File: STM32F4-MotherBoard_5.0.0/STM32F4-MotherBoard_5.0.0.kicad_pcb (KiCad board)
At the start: 2 copper layers, 95 parts, among them J1 RJ45, J2 RJ45, J3 RJ12, J4 RJ12, P1 VCC, P2 GND, P3 DIO0, P4 ADC, P5 DIO1, P6 SWD, P7 ENC0, P8 ENC2, P9 ENC1, SW1 ON/OFF, SW2 Reset, SW3 SW_PUSH, SW4 SW_ROTARY, SW5 WRITE/RUN, U1 STM32F407VG, U2 OKL-T6-W12, U3 PQ033EZ1H, U4 MCP2551-I/SN, U5 ADM3202, U6 AS021350D, Y1 8MHz

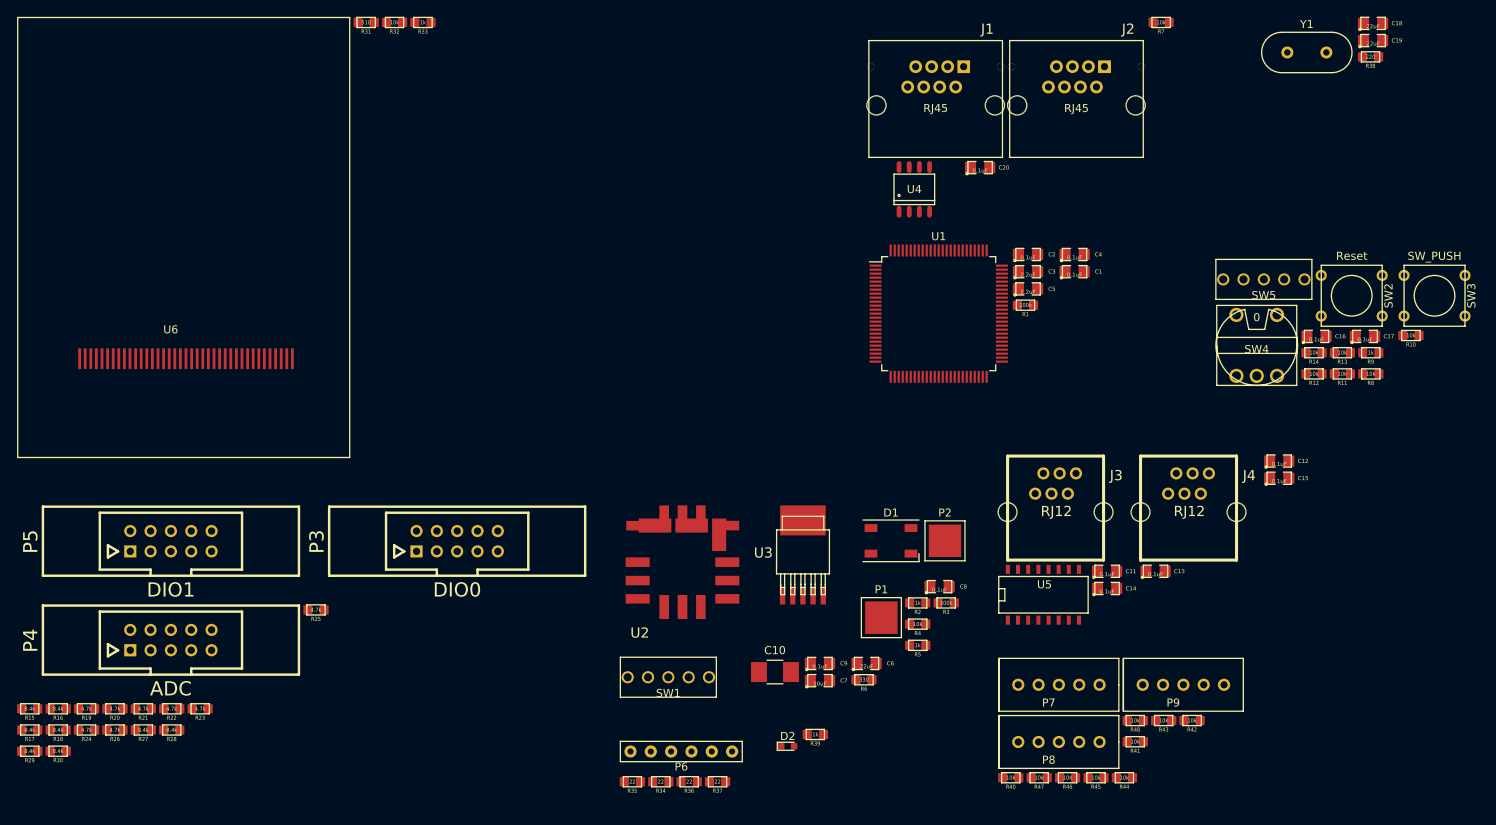
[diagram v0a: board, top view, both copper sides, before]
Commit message: 部品配置終わり
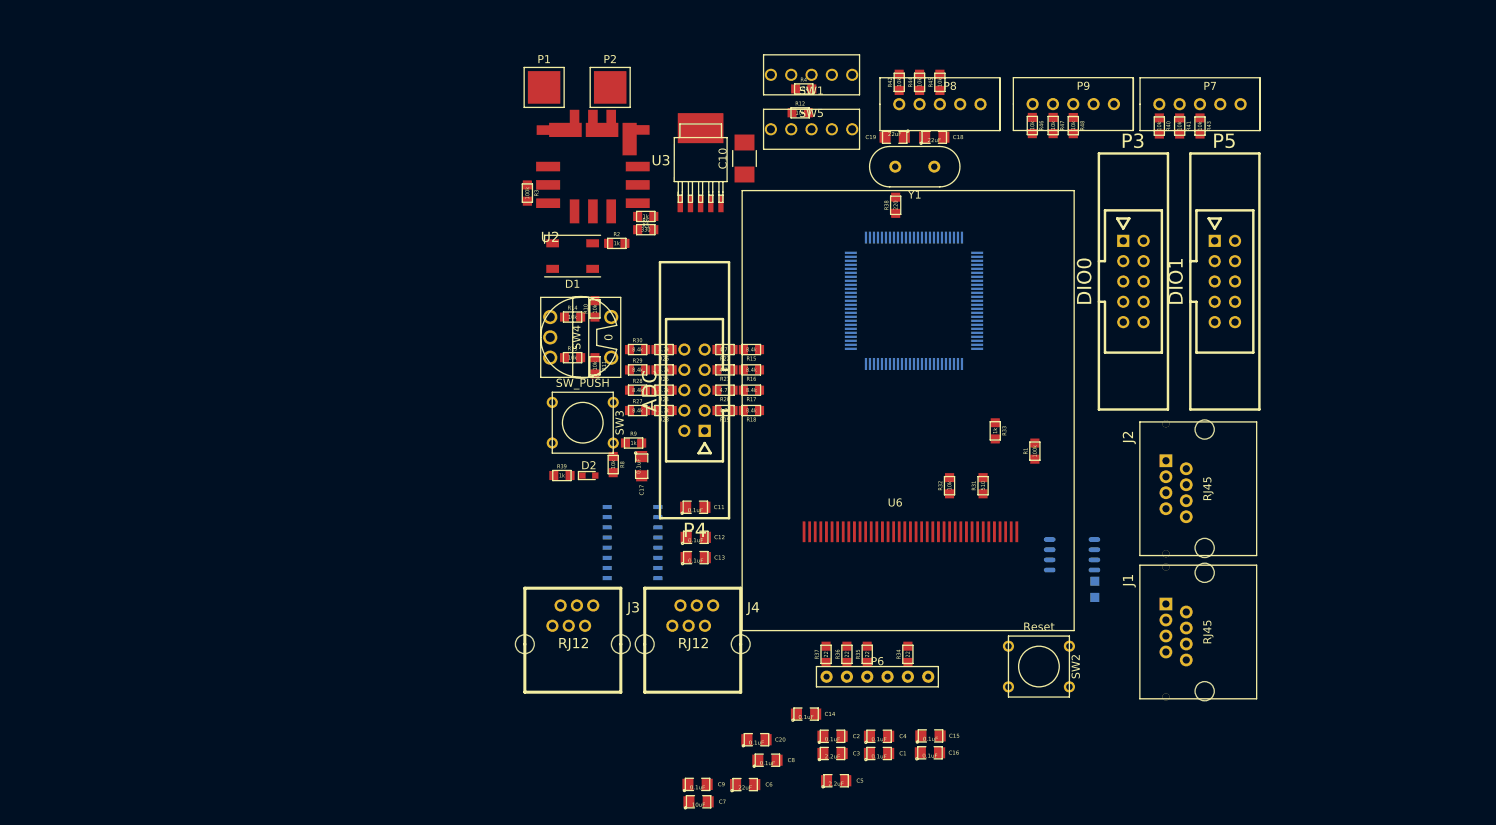
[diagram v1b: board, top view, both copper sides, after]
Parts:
- R7, U1, U4, U5: moved to B.Cu
- moved P5 135.7 mm to (204.5, 66.7), turned to 270 degrees
- moved SW3 107.6 mm to (124.2, 84.3)
- moved R10 102.1 mm to (125.7, 70.1), turned to 270 degrees
- moved R15 100.8 mm to (145.3, 75.2)
- moved R17 99.7 mm to (145.3, 80.3)
- moved R16 96.5 mm to (145.3, 77.7)
- moved R31 96.4 mm to (174.2, 92.2), turned to 270 degrees
- moved R13 96.2 mm to (122.9, 76.2), turned to 180 degrees
- moved R18 95.4 mm to (145.3, 82.8)
- moved R8 95.4 mm to (128.0, 89.6), turned to 90 degrees
- moved R11 93.4 mm to (125.7, 77.2), turned to 90 degrees
- moved U6 93.1 mm to (151.1, 99.3)
- moved R9 92.8 mm to (130.6, 86.9), turned to 180 degrees
- moved R14 92.8 mm to (122.9, 71.1), turned to 180 degrees
- moved C17 91.9 mm to (131.6, 89.8), turned to 270 degrees
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
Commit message: 部品配置再考終わり
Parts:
- added REF**: 1pin, Connect:1pin, F.Cu at (163.8, 50.8)
- added REF**: 1pin, Connect:1pin, F.Cu at (163.8, 127.0)
- added REF**: 1pin, Connect:1pin, F.Cu at (75.6, 50.8)
- added REF**: 1pin, Connect:1pin, F.Cu at (75.6, 127.0)
- C11, C12, C13, C14, C3, R1, R12, R15, R16, R17, R18, R19, R20, R21, R22, R23, R24, R25, R26, R27, R28, R29, R30, R38, R4, R40, R41, R42, R43, R44, R45: moved to B.Cu
- R7, U4: moved to F.Cu
- moved P5 123.7 mm to (83.2, 90.6), turned to 90 degrees
- moved P3 101.3 mm to (94.5, 90.4), turned to 90 degrees
- moved C6 98.9 mm to (75.6, 58.6), turned to 180 degrees
- moved C15 85.9 mm to (98.7, 72.2), turned to 180 degrees
- moved C1 85.2 mm to (101.5, 64.9), turned to 270 degrees
- moved C20 82.4 mm to (91.9, 61.8), turned to 270 degrees
- moved C8 81.9 mm to (91.6, 66.4), turned to 270 degrees
- moved P7 81.1 mm to (120.7, 52.7), turned to 0 degrees
- moved R43 81.1 mm to (120.7, 55.3)
- moved C2 76.9 mm to (105.6, 64.9), turned to 270 degrees
- moved R41 76.1 mm to (123.2, 55.3)
- moved C7 74.6 mm to (93.8, 72.2), turned to 180 degrees
- moved C9 73.5 mm to (103.5, 64.9), turned to 270 degrees
- moved R40 71.0 mm to (125.7, 55.4)
- moved R14 66.0 mm to (78.6, 120.0), turned to 0 degrees
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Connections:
- C20 pad 1: +5VP -> +5V
- U4 pad 3: +5VP -> +5V
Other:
- board outline added: 95.9 x 83.8 mm
- net class Default: clearance 0.2 -> 0.15; trace_width 0.25 -> 0.203
- rule trace_clearance: 0.2 -> 0.15

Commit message: ミス
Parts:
- ? (x4): renamed from REF**; value 1pin -> (none)
- C4: moved to B.Cu
- moved C4 16.5 mm to (137.3, 116.2)
- moved C5 13.7 mm to (105.6, 102.2), turned to 225 degrees
- moved R33 10.8 mm to (133.9, 109.7), turned to 270 degrees
- moved C3 6.41 mm to (132.3, 94.1), turned to 225 degrees
- moved R8 5.02 mm to (80.4, 112.2)
- moved R10 2.05 mm to (92.2, 121.0), turned to 90 degrees
- moved R31 1.76 mm to (133.9, 106.2)
- moved C17 1.14 mm to (78.4, 111.9)
- moved R1 0.97 mm to (138.0, 85.7)
- moved R9 0.82 mm to (79.4, 115.1), turned to 0 degrees
- moved + 0.57 mm to (79.4, 55.1)
- moved R4 0.30 mm to (105.7, 53.4)
- turned P5 to 270 degrees
- turned P3 to 270 degrees
- renumbered P1 to +, P2 to -, J1 to CAN, J2 to CAN, J4 to Communication, J3 to Controller, P7 to ENC0, P9 to ENC1, P8 to ENC2, D2 to LED, SW1 to ON/OFF, D1 to Pow, P6 to ST-Link, SW5 to WRITE/RUN
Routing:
- net +3V3: track 0.00 -> 503.4 mm, vias 0 -> 12
- net GND: track 0.00 -> 211.4 mm, vias 0 -> 12
- net +5V: track 0.00 -> 208.9 mm, vias 0 -> 3
- net +12V: track 0.00 -> 136.4 mm
- net RotarySW2: track 0.00 -> 90.6 mm, vias 0 -> 2
- net RotarySW3: track 0.00 -> 84.8 mm, vias 0 -> 2
- net ADC4: track 0.00 -> 83.0 mm, vias 0 -> 2
- net ADC5: track 0.00 -> 77.8 mm, vias 0 -> 2
- net SWO: track 0.00 -> 71.3 mm, vias 0 -> 3
- net PushSW: track 0.00 -> 71.2 mm, vias 0 -> 3
- net ADC2: track 0.00 -> 70.8 mm, vias 0 -> 2
- net ENC2_Z: track 0.00 -> 69.2 mm, vias 0 -> 2
- net ADC6: track 0.00 -> 66.3 mm, vias 0 -> 2
- net ADC0: track 0.00 -> 66.2 mm, vias 0 -> 2
- net ADC1: track 0.00 -> 66.1 mm, vias 0 -> 2
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- added copper zone on B.Cu, net GND
- added copper zone on F.Cu, net GND
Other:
- board text added: "Designed with KiCAD by mugi"

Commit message: replace project
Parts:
- added J5: DM3AT-SF-PEJM5, HRS_DM3AT-SF-PEJM5, B.Cu at (125.0, 114.4)
- LED: value LED -> (none)
- moved R27 2.94 mm to (106.6, 113.0)
- moved R20 2.94 mm to (109.1, 124.5)
- moved R19 2.94 mm to (106.6, 124.5)
- moved R21 2.94 mm to (111.6, 124.5)
- moved R23 2.94 mm to (106.6, 116.6)
- moved R22 2.94 mm to (114.2, 124.5)
- moved R17 2.93 mm to (109.1, 128.0)
- moved R18 2.93 mm to (106.6, 128.0)
- moved R15 2.93 mm to (114.2, 128.0)
- moved R16 2.93 mm to (111.6, 128.0)
- moved R29 2.93 mm to (111.6, 113.0)
- moved R28 2.93 mm to (109.1, 113.0)
- moved R30 2.93 mm to (114.2, 113.0)
- moved R25 2.92 mm to (111.6, 116.6)
- moved R24 2.92 mm to (109.1, 116.6)
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- renumbered Communication to ←Communication, Controller to →Controller
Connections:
- net +3.3VP renamed +12VA
- CAN pad 3: +5VP -> +5V (x2)
- CAN pad 4: +5VP -> +5V (x2)
- U1 pad 52: (no net) -> SPI_SCK
- U1 pad 53: (no net) -> SPI_MISO
- U1 pad 54: (no net) -> SPI_MOSI
- U1 pad 7: (no net) -> SPI_CS
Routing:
- net GND: track 211.4 -> 671.7 mm, vias 12 -> 61
- net +5V: track 208.9 -> 360.3 mm
- net SPI_CS: track 0.00 -> 94.1 mm, vias 0 -> 6
- net SPI_MISO: track 0.00 -> 34.9 mm, vias 0 -> 4
- net SPI_MOSI: track 0.00 -> 34.1 mm, vias 0 -> 4
- net SPI_SCK: track 0.00 -> 32.9 mm, vias 0 -> 4
- net +5VP: track 27.6 -> 0.00 mm
- net +3V3: track 503.4 -> 494.0 mm
- net ADC6: track 66.3 -> 74.2 mm
- net ADC4: track 83.0 -> 88.8 mm
- net ADC2: track 70.8 -> 74.8 mm
- net ADC5: track 77.8 -> 81.5 mm
- net FSMC_D13: track 16.9 -> 13.9 mm
- net ADC7: track 57.9 -> 60.8 mm
- net ADC1: track 66.1 -> 68.9 mm
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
